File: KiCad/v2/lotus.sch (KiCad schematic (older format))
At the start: 30 parts, among them J1 USB_B_Micro, J2 Conn_01x04, J3 Conn_01x02, SW1 SW_Push, SW2 SW_Push, U1 BQ24072, U2 ESP-12E, U3 MIC5504-3.3YM5, U4 Battery

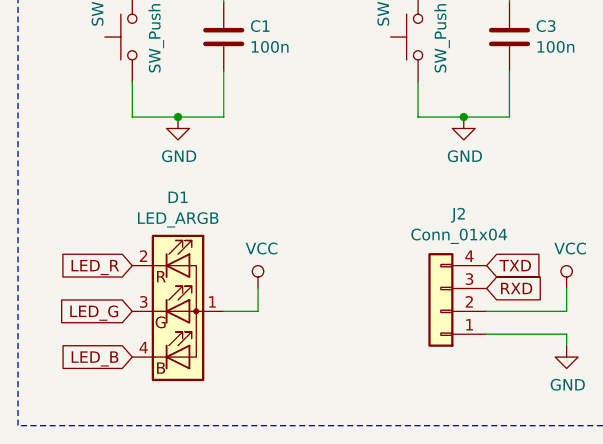
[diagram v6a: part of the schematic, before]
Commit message: Adicionado resistores no led
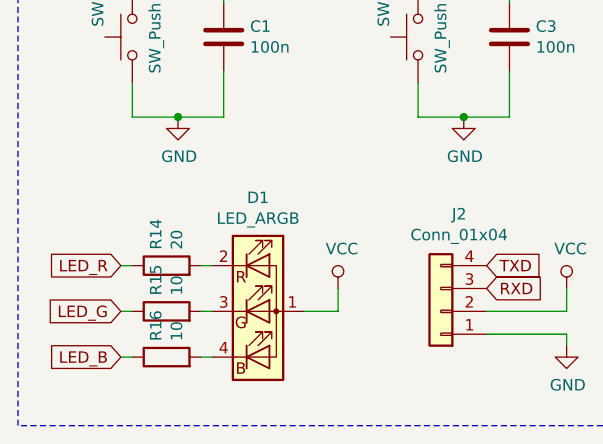
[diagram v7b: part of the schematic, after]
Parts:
- added R14: 20, Resistor_SMD:R_0402_1005Metric, symbol Device:R
- added R15, R16: 10, Resistor_SMD:R_0402_1005Metric, symbol Device:R
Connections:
- net LED_B: now also R16.1; no longer D1.4 (BK)
- net LED_G: now also R15.1; no longer D1.3 (GK)
- net LED_R: now also R14.1; no longer D1.2 (RK)
- new net: D1.2 (RK), R14.2
- new net: D1.3 (GK), R15.2
- new net: D1.4 (BK), R16.2
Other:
- moved on the sheet: D1
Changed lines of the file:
@@
 L Device:LED_ARGB D1
 U 1 1 5BDC7C40
-P 1800 6000
-F 0 "D1" H 1800 6497 50  0000 C CNN
-F 1 "LED_ARGB" H 1800 6406 50  0000 C CNN
-F 2 "LED_SMD:LED_Cree-PLCC4_3.2x2.8mm_CCW" H 1800 5950 50  0001 C CNN
-F 3 "~" H 1800 5950 50  0001 C CNN
-	1    1800 6000
-	1    0    0    -1
-$EndComp
-Text GLabel 1600 5800 0    50   Input ~ 0
+P 2150 6000
+F 0 "D1" H 2150 6497 50  0000 C CNN
+F 1 "LED_ARGB" H 2150 6406 50  0000 C CNN
+F 2 "LED_SMD:LED_Cree-PLCC4_3.2x2.8mm_CCW" H 2150 5950 50  0001 C CNN
+F 3 "~" H 2150 5950 50  0001 C CNN
+	1    2150 6000
+	1    0    0    -1
+$EndComp
+Text GLabel 1550 5800 0    50   Input ~ 0
 LED_R
-Text GLabel 1600 6000 0    50   Input ~ 0
+Text GLabel 1550 6000 0    50   Input ~ 0
 LED_G
-Text GLabel 1600 6200 0    50   Input ~ 0
+Text GLabel 1550 6200 0    50   Input ~ 0
 LED_B
 Text GLabel 6050 5250 2    50   Input ~ 0
@@
 L power:VCC #PWR0112
 U 1 1 5BDDA17C
-P 2150 5900
-F 0 "#PWR0112" H 2150 5750 50  0001 C CNN
-F 1 "VCC" H 2167 6073 50  0000 C CNN
-F 2 "" H 2150 5900 50  0001 C CNN
-F 3 "" H 2150 5900 50  0001 C CNN
-	1    2150 5900
-	1    0    0    -1
-$EndComp
-Wire Wire Line
-	2150 5900 2150 6000
-Wire Wire Line
-	2150 6000 2000 6000
+P 2500 5900
+F 0 "#PWR0112" H 2500 5750 50  0001 C CNN
+F 1 "VCC" H 2517 6073 50  0000 C CNN
+F 2 "" H 2500 5900 50  0001 C CNN
+F 3 "" H 2500 5900 50  0001 C CNN
+	1    2500 5900
+	1    0    0    -1
+$EndComp
+Wire Wire Line
+	2500 5900 2500 6000
+Wire Wire Line
+	2500 6000 2350 6000
 $Comp
 L Lotus-rescue:BQ24072-Battery_Management U1
@@
 Wire Wire Line
 	5250 1750 5050 1750
+$Comp
+L Device:R R14
+U 1 1 5C0971A6
+P 1750 5800
+F 0 "R14" H 1820 5846 50  0000 L CNN
+F 1 "20" H 1820 5755 50  0000 L CNN
+F 2 "Resistor_SMD:R_0402_1005Metric" V 1680 5800 50  0001 C CNN
+F 3 "~" H 1750 5800 50  0001 C CNN
+	1    1750 5800
+	0    -1   -1   0
+$EndComp
+$Comp
+L Device:R R15
+U 1 1 5C09747D
+P 1750 6000
+F 0 "R15" H 1820 6046 50  0000 L CNN
+F 1 "10" H 1820 5955 50  0000 L CNN
+F 2 "Resistor_SMD:R_0402_1005Metric" V 1680 6000 50  0001 C CNN
+F 3 "~" H 1750 6000 50  0001 C CNN
+	1    1750 6000
+	0    -1   -1   0
+$EndComp
+$Comp
+L Device:R R16
+U 1 1 5C0974D1
+P 1750 6200
+F 0 "R16" H 1820 6246 50  0000 L CNN
+F 1 "10" H 1820 6155 50  0000 L CNN
+F 2 "Resistor_SMD:R_0402_1005Metric" V 1680 6200 50  0001 C CNN
+F 3 "~" H 1750 6200 50  0001 C CNN
+	1    1750 6200
+	0    -1   -1   0
+$EndComp
+Wire Wire Line
+	1900 6200 1950 6200
+Wire Wire Line
+	1600 6200 1550 6200
+Wire Wire Line
+	1550 6000 1600 6000
+Wire Wire Line
+	1900 6000 1950 6000
+Wire Wire Line
+	1950 5800 1900 5800
+Wire Wire Line
+	1600 5800 1550 5800
 $EndSCHEMATC
